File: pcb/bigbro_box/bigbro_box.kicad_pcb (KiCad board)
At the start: 2 copper layers, 112 x 55 mm, 49 parts, among them J1 CT_AMP, J2 RFID, J3 Mains, J4 UART flashing, J5 Conn_01x24_MountingPin, J6 RELAY, K1 G5LE-1, Q1 MUN5211DW1, Q2 Q_NMOS_GDS, Q3 Si1308EDL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

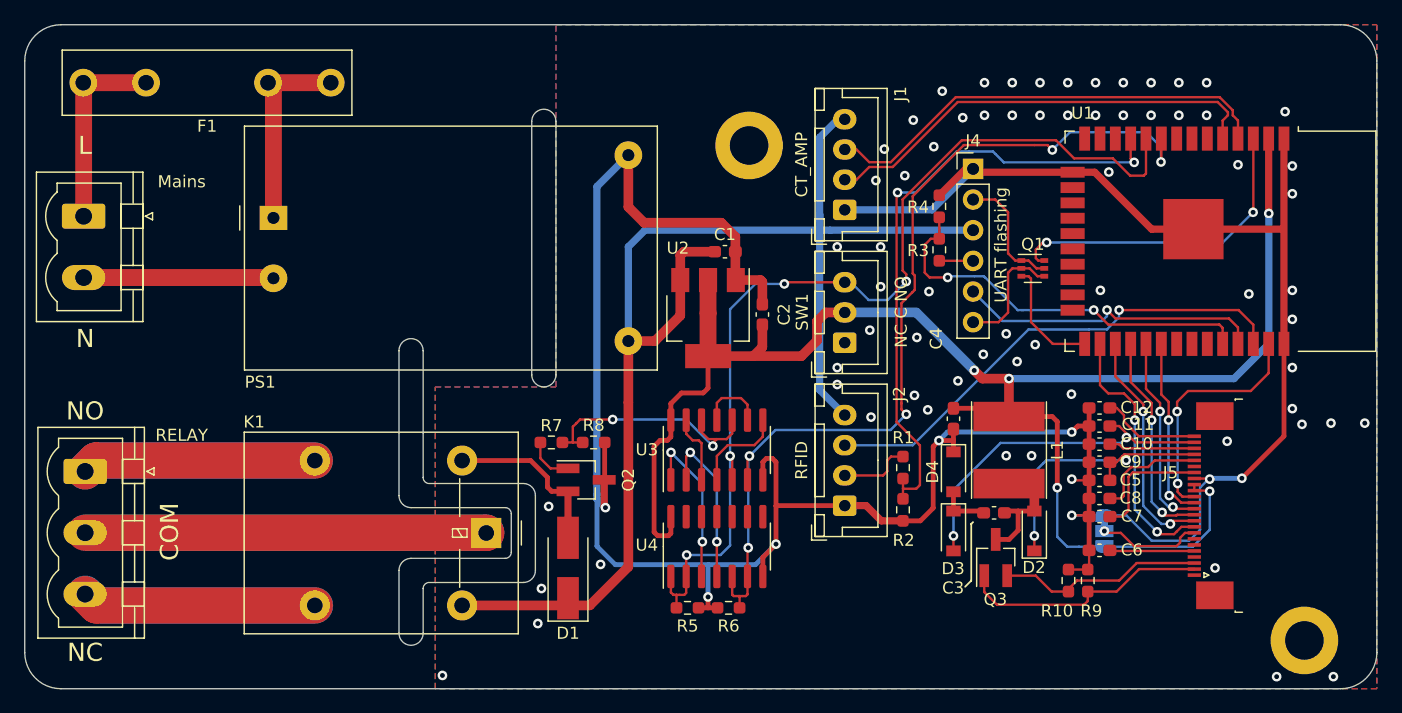
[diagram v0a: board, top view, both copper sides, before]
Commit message: Widened isolation slot
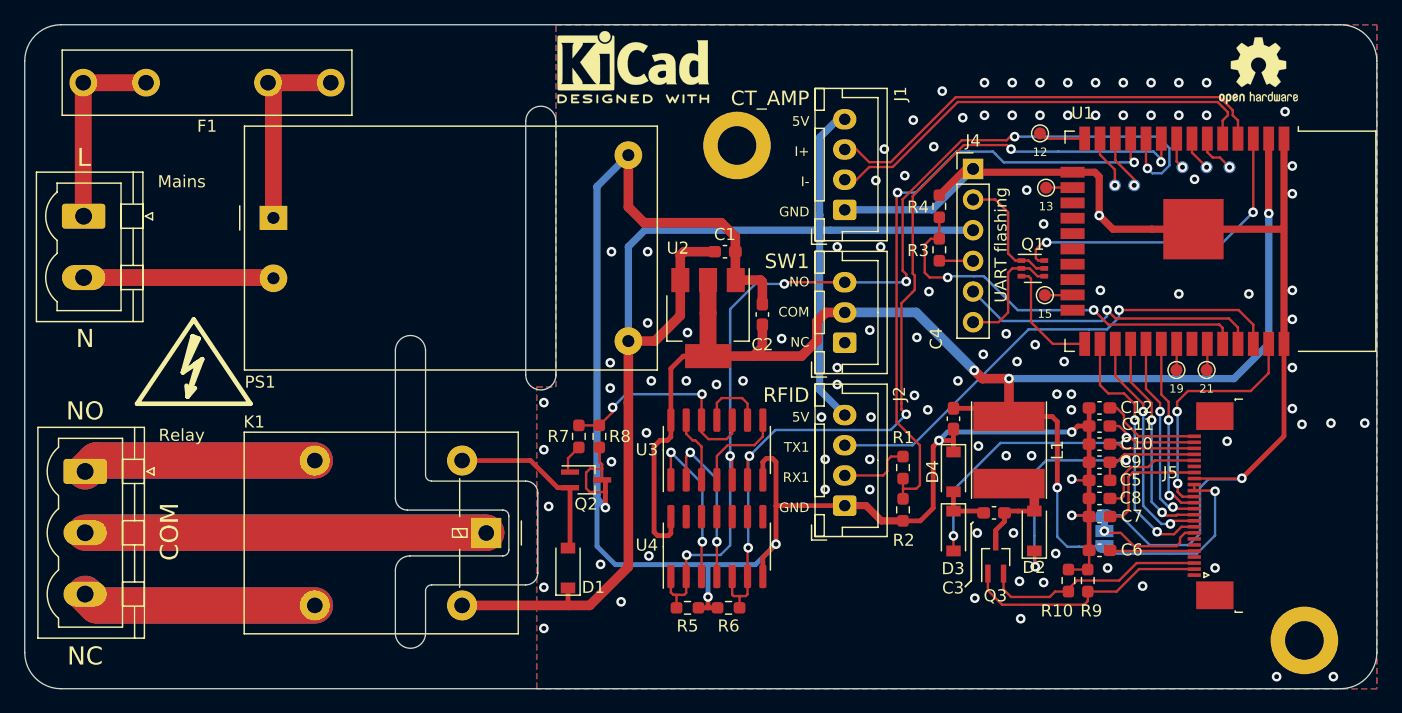
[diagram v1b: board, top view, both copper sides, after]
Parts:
- added REF**: KiCad-Logo2_5mm_SilkScreen, Symbol:KiCad-Logo2_5mm_SilkScreen, F.Cu at (110.4, 63.5)
- added REF**: OSHW-Logo2_7.3x6mm_SilkScreen, Symbol:OSHW-Logo2_7.3x6mm_SilkScreen, F.Cu at (162.2, 63.8)
- added REF**: Symbol_HighVoltage_Type2_CopperTop_VerySmall, Symbol:Symbol_HighVoltage_Type2_CopperTop_VerySmall, F.Cu at (74.0, 88.6)
- added REF**: Symbol_HighVoltage_Type2_CopperTop_VerySmall, Symbol:Symbol_HighVoltage_Type2_CopperTop_VerySmall, B.Cu at (74.0, 88.6)
- added REF**: KiCad-Logo2_5mm_SilkScreen, Symbol:KiCad-Logo2_5mm_SilkScreen, B.Cu at (110.4, 63.5)
- added REF**: OSHW-Logo2_7.3x6mm_SilkScreen, Symbol:OSHW-Logo2_7.3x6mm_SilkScreen, B.Cu at (162.2, 63.8)
- added TP1: 12, TestPoint:TestPoint_Pad_D1.0mm, F.Cu at (144.1, 69.0)
- added TP10: 35, TestPoint:TestPoint_Pad_D1.0mm, B.Cu at (157.9, 71.8)
- added TP2: 13, TestPoint:TestPoint_Pad_D1.0mm, F.Cu at (144.6, 73.5)
- added TP3: 14, TestPoint:TestPoint_Pad_D1.0mm, B.Cu at (150.3, 73.3)
- added TP4: 15, TestPoint:TestPoint_Pad_D1.0mm, F.Cu at (144.5, 82.4)
- added TP5: 19, TestPoint:TestPoint_Pad_D1.0mm, F.Cu at (155.4, 88.6)
- added TP6: 21, TestPoint:TestPoint_Pad_D1.0mm, F.Cu at (157.9, 88.6)
- added TP7: 27, TestPoint:TestPoint_Pad_D1.0mm, B.Cu at (151.9, 73.3)
- added TP8: 32, TestPoint:TestPoint_Pad_D1.0mm, B.Cu at (155.9, 71.8)
- added TP9: 34, TestPoint:TestPoint_Pad_D1.0mm, B.Cu at (159.8, 71.8)
- D1: footprint Diode_SMD:D_SMA_Handsoldering -> Diode_SMD:D_SOD-123
- J5: value Conn_01x24_MountingPin -> 2-1734839-4
- J6: value RELAY -> Relay
- Q2, Q3: footprint Package_TO_SOT_SMD:SOT-23_Handsoldering -> Package_TO_SOT_SMD:SOT-323_SC-70_Handsoldering
- moved R7 2.33 mm to (105.9, 94.1), turned to -90 degrees
- moved REF** 1.00 mm to (119.0, 70.0)
- moved R8 0.69 mm to (107.6, 94.1), turned to -90 degrees
- moved G*** 0.21 mm to (127.5, 107.5)
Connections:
- J5 pad MP: unconnected-(J5-PadMP) -> GND
- U1 pad 12: unconnected-(U1-Pad12) -> Net-(U1-Pad12)
- U1 pad 13: unconnected-(U1-Pad13) -> Net-(U1-Pad13)
- U1 pad 14: unconnected-(U1-Pad14) -> Net-(U1-Pad14)
- U1 pad 16: unconnected-(U1-Pad16) -> Net-(U1-Pad16)
- U1 pad 23: unconnected-(U1-Pad23) -> Net-(U1-Pad23)
- U1 pad 31: unconnected-(U1-Pad31) -> Net-(U1-Pad31)
- U1 pad 33: unconnected-(U1-Pad33) -> Net-(U1-Pad33)
- U1 pad 6: unconnected-(U1-Pad6) -> Net-(U1-Pad6)
- U1 pad 7: unconnected-(U1-Pad7) -> Net-(U1-Pad7)
- U1 pad 8: unconnected-(U1-Pad8) -> Net-(U1-Pad8)
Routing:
- net GND: track 260.4 -> 269.6 mm, vias 76 -> 111
- net Net-(U1-Pad12): track 0.00 -> 4.51 mm, vias 0 -> 1
- net Net-(U1-Pad13): track 0.00 -> 4.38 mm, vias 0 -> 1
- net Net-(U1-Pad14): track 0.00 -> 3.88 mm
- net Net-(U1-Pad6): track 0.00 -> 3.48 mm, vias 0 -> 1
- net /card_switch: track 82.5 -> 85.8 mm, vias 4 -> 6
- net Net-(U1-Pad7): track 0.00 -> 2.87 mm, vias 0 -> 1
- net /relay: track 21.6 -> 18.8 mm
- net /Display/VGH: track 23.8 -> 26.5 mm
- net Net-(U1-Pad8): track 0.00 -> 2.57 mm, vias 0 -> 1
- net Net-(U1-Pad23): track 0.00 -> 2.31 mm
- net Net-(U1-Pad16): track 0.00 -> 2.20 mm
- net Net-(U1-Pad33): track 0.00 -> 2.19 mm
- net Net-(U1-Pad31): track 0.00 -> 2.17 mm
- net Net-(Q2-Pad1): track 3.95 -> 2.11 mm
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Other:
- outline, holes or cut-outs redrawn
- board text added: "5V"
- board text added: "GND"
- board text added: "I+"
- board text added: "I-"
- board text added: "RX1"
- board text added: "TX1"
- board text removed: "NC C NO"

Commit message: Order1
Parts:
- added G***: LOGO, hal9k-graphics:hal9k-logo_20mm, F.Cu at (148.5, 111.7)
- added G***: LOGO, hal9k-graphics:hal9k-logo_20mm, B.Cu at (148.5, 111.7)
- C1: value 10uF -> 1uF
- C2: value 1uF -> 10uF
- Q1: value MUN5211DW1 -> ADC114YUQ
- R1, R3: value 4k7 -> 1k2
- R2, R4: value 9k1 -> 2k2
- moved REF** 74.2 mm to (106.1, 112.4) (x2)
- moved G*** 1.60 mm to (131.5, 109.1)
- moved G*** 1.60 mm to (127.5, 109.1)
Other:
- board text added: "GND GND"
- board text added: "git.io/bigbro"
